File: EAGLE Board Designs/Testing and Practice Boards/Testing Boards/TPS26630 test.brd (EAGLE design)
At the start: 100 x 80 mm, 3 parts

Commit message: Finished the TPS26630 E-Fuse breakout board layout
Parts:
- moved JP2 31.9 mm to (22.9, 14.0), turned to 90 degrees
- moved TPS26630-1 21.8 mm to (14.0, 14.0), flipped to the bottom, turned to 180 degrees
- moved JP1 13.7 mm to (5.08, 14.0), turned to 270 degrees
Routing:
- net GND: track 0.00 -> 12.3 mm
- net ILIM: track 0.00 -> 9.93 mm
- net DVDT: track 0.00 -> 9.93 mm
- net IN: track 0.00 -> 9.77 mm
- net OUT: track 0.00 -> 9.77 mm
- net B_GATE: track 0.00 -> 9.11 mm
- net PGOOD: track 0.00 -> 9.07 mm
- net MODE: track 0.00 -> 7.67 mm
- net DRV: track 0.00 -> 7.44 mm
- net PGTH: track 0.00 -> 7.44 mm
- net OVP: track 0.00 -> 6.89 mm
- net SHDN: track 0.00 -> 6.89 mm
- net IN_SYS: track 0.00 -> 6.66 mm
- net FLT: track 0.00 -> 6.66 mm
- net UVLO: track 0.00 -> 6.11 mm
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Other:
- board size 100 x 80 mm -> 27.6 x 27.9 mm

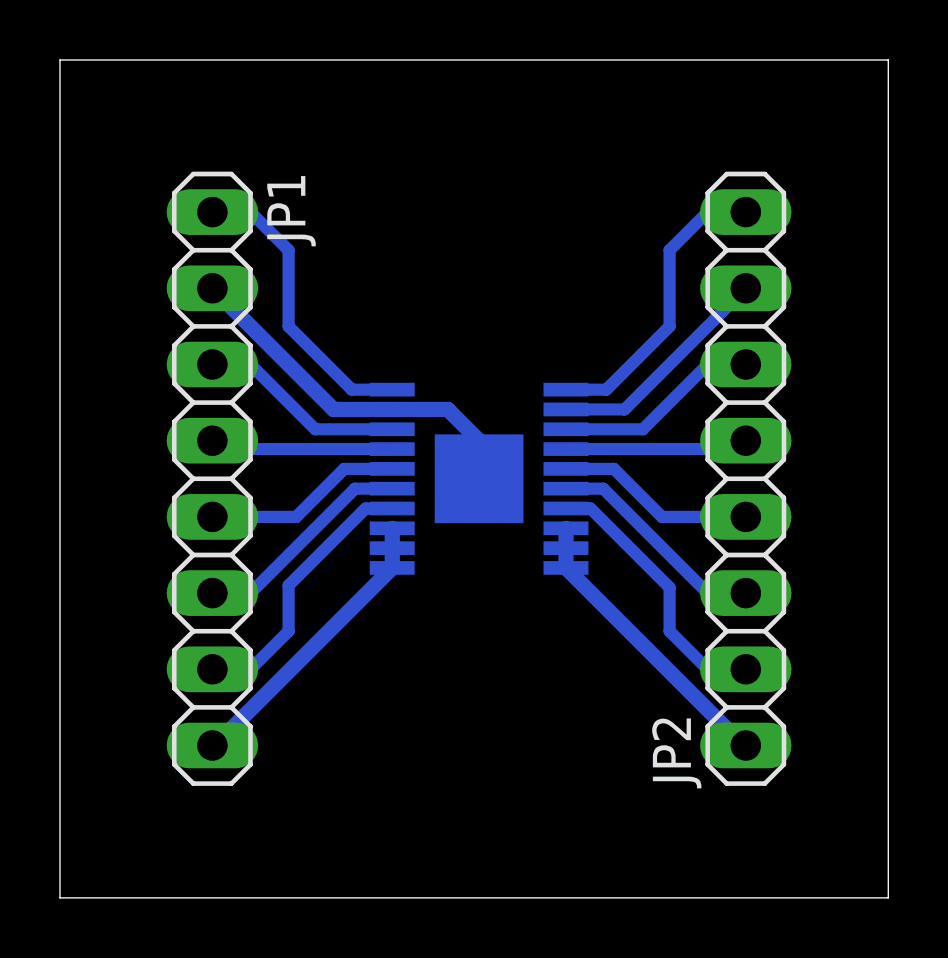
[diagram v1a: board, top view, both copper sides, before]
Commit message: Made changes to the TPS26630 test board so that it is ready to be manufactured
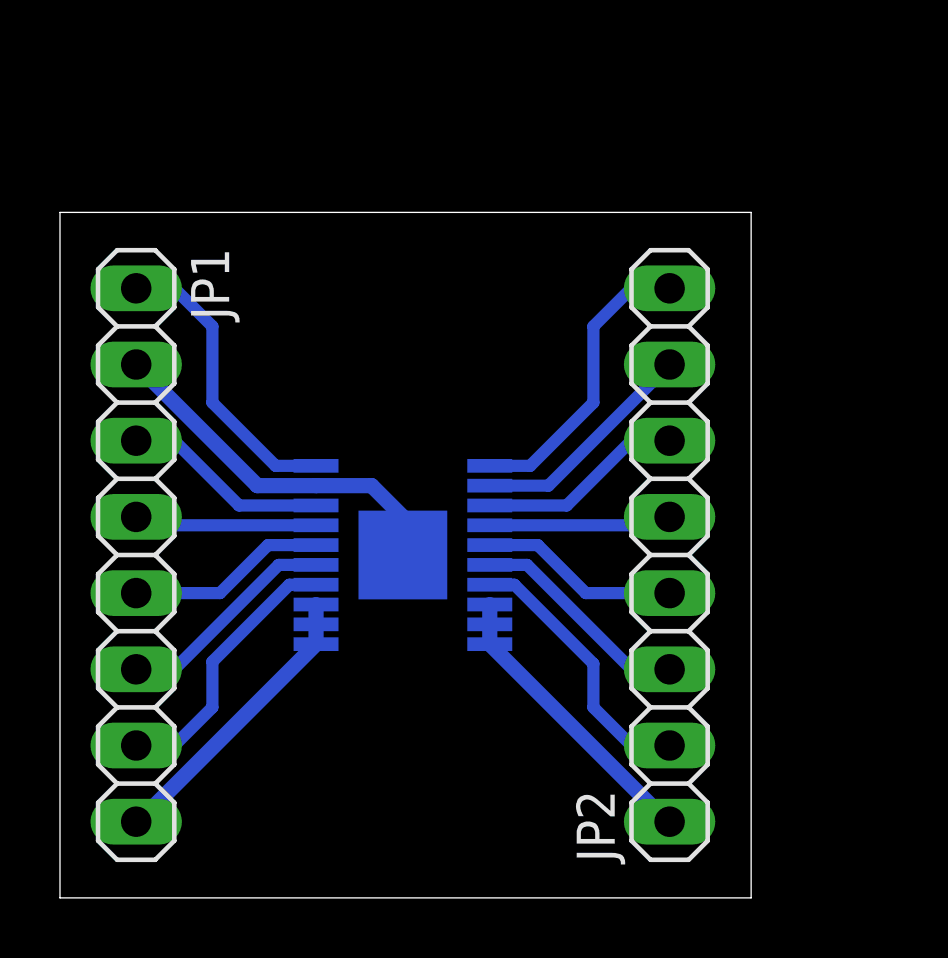
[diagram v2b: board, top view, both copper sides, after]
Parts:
- moved TPS26630-1 3.59 mm to (11.4, 11.4)
- moved JP1 3.59 mm to (2.54, 11.4)
- moved JP2 3.59 mm to (20.3, 11.4)
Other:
- board size 27.6 x 27.9 mm -> 23 x 22.9 mm
